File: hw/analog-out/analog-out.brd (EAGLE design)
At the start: 90.2 x 37 mm, 126 parts

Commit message: First verision of dac schematic
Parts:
- removed ADC_: LTC2312, LTC2312-14:TSOT-23_TS8_LIT
- removed ADC_IN, ADC_REF, A_IN, FILTER: TESTPIN, myLib:1X01
- removed ANALOG_IN: PTR1B1,27, testpad:B1,27
- removed C15, C18, C19: 2u2, rcl:C0805K
- removed C8: 100n, rcl:C0805K
- removed C_FILTER: 330p, rcl:C0805K
- removed C_FILTER1: nb, rcl:C0805K
- removed INSTR_AMP: AD8250ARMZ, parts:RM_10_ADI
- removed LED2: GREEN, led:SML0805
- removed MINUS, PLUS: 23.3200-21, CONN_BANANA_JACK_4MM_STAUBLI:CONN_23.3200-21_SBI
- removed MOV1: CV300CVQ300K10BL1, myLib:CVQ300K10
- removed PIN_HEADER_SMD: (no value), SMD10_2_pinheader:MA05-2
- removed R11: 0, rcl:R0805
- removed R12: 47k, rcl:R0805
- removed R13: inf, rcl:R0805
- removed R14, R_FILTER1: nb, rcl:R0805
- removed R53, R57, R58: nb, rcl:R1206
- removed R_FILTER: 2k2, rcl:R0805
- added C27: 10p, rcl:C0805
- added C28, C29: 100n, rcl:C0805
- added CONV1: PTR1B1,27, testpad:B1,27
- added POWER1: gr, led:SML0805
- added R23: 680, resistor:R0805
- added U$3: ADA4522-2ARZ-RL, my:MSOP8
- added U$4: MAX1036EKA+T, my:SOT23-8L
- added U$5: 73099RED, my:4MM_BANANA
- added U$6: 73099BLACK, my:4MM_BANANA
- C5: device rcl:C0805K -> rcl:C0805
- R10: value 390k -> tbd
- R3: value 680 -> tbd
- R4, R5: value nb -> tbd; device rcl:R1206 -> rcl:R0805
- U$1: value 0508.500MXEP -> LTC2642IMS-16; device 0508.500MXEP.FUSE:0508.500MXEP -> my:MSOP10
- moved R10 100.7 mm to (-38.2, -48.8), turned to 0 degrees
- moved R3 94.5 mm to (-38.2, -42.5), flipped to the top
- moved R19 91.9 mm to (57.4, 20.4), turned to 90 degrees
- moved C5 87.1 mm to (-38.2, -36.3), flipped to the top, turned to 0 degrees
- moved R18 86.5 mm to (55.2, 20.4), turned to 90 degrees
- moved R5 72.4 mm to (-30.7, -30.1), turned to 0 degrees
- moved R8 71.3 mm to (35.6, 26.8), turned to 180 degrees
- moved R4 58.2 mm to (-30.7, -23.9), turned to 0 degrees
- moved U$1 46.3 mm to (-21.6, 1.02), turned to 0 degrees
- moved R22 42.2 mm to (70.5, 16.6)
- moved R20 34.4 mm to (71.1, 21.3), turned to 90 degrees
- moved STATUS 31.0 mm to (42.2, 18.5), turned to 180 degrees
- moved +5V 10.2 mm to (50.0, 29.5)
- moved C6 7.39 mm to (69.1, 22.0), turned to 90 degrees
- moved GOLD_ORB_SM1 2.74 mm to (40.8, 30.1), turned to 180 degrees
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- renumbered REF_2.048 to REF_2.5
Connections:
- removed net >ADC: ADC_.4, ADC_IN.1, C_FILTER.1, R10.2, R11.2, R_FILTER.1
- removed net CONV<: PIN_HEADER_SMD.6, RJ45.5
- removed net CONV>: CONVERSION.2, PIN_HEADER_SMD.1
- removed net GAIN_LSB: INSTR_AMP.4, U$2.11
- removed net GAIN_MSB: INSTR_AMP.5, U$2.12
- removed net N$18: R11.1, R13.2, SATURATION_DETECT.3
- removed net N$20: ANALOG_IN.TP, A_IN.1, R14.2, R4.1, U$20.6
- removed net N$21: R57.1, R58.2
- removed net N$29: R4.2, R53.1
- removed net N$4: I2C.3, R18.1, ROHM_I2C.6, U$2.14
- removed net N$6: I2C.2, R19.1, ROHM_I2C.5, U$2.15
- removed net N$66: R53.2, R58.1
- removed net N$67: R5.1, R57.2
- removed net N$8: ADC_.2, ADC_REF.1, C19.2
- removed net N_STATUS_LED: R8.1, U$2.6
- removed net SAT_DETECT: R3.1, SATURATION_DETECT.1, SATURATION_DETECT.6, U$2.10
- removed net SCL<: PIN_HEADER_SMD.5, RJ45.7
- removed net SCL>: I2C.6, PIN_HEADER_SMD.2, R22.1
- removed net SDO<: PIN_HEADER_SMD.4, RJ45.8
- removed net SDO>: I2C.7, PIN_HEADER_SMD.3, R20.1
- new net ANALOG_FEEDBACK: U$20.1, U$4.1
- new net CONV: CONV1.TP, CONVERSION.2, RJ45.5
- new net N$22: R8.1, STATUS.A
- new net N$27: POWER1.A, R23.1
- new net SCL: I2C.6, R22.1, RJ45.7
- new net SDO: I2C.7, R20.1, RJ45.8
- new net STATUS_LED: R8.2, U$2.6
- new net V_OUT: R10.1, R4.2, TP1.TP, TP3.TP, U$3.7, U$5.P$1
- net +5V: now also C28.1, C29.1, C5.1, R23.2, U$1.9, U$3.4, U$4.8; no longer ADC_.1, ADC_.5, C15.1, C18.1, C5.2, INSTR_AMP.8, LED2.A, STATUS.A
- net -5V: now also C28.2, U$3.8; no longer C8.2, INSTR_AMP.3
- net CONV_ADC: now also U$1.2; no longer ADC_.8
- net DGND: now also C29.2, C5.2, POWER1.C, R3.2, R5.2, STATUS.C, U$1.10, U$4.7, U$6.P$1; no longer ADC_.3, C15.2, C18.2, C19.1, C5.1, C8.1, C_FILTER.2, C_FILTER1.2, INSTR_AMP.1, INSTR_AMP.2, MINUS.1, MOV1.2, R12.1, R13.1, R14.1
- net N$1: now also C27.2, U$1.7, U$3.2; no longer INSTR_AMP.7, R_FILTER.2
- net N$14: now also I2C.2, R19.1, ROHM_I2C.5, U$2.15, U$4.6; no longer LED2.C, R3.2
- net N$15: now also R4.1, R5.1, U$3.6; no longer C_FILTER1.1, INSTR_AMP.10, R_FILTER1.1
- net N$16: now also R10.2, R3.1, U$20.6; no longer PLUS.1, TP1.TP, TP3.TP, U$1.P$1
- net N$17: now also I2C.3, R18.1, ROHM_I2C.6, U$2.14, U$4.5; no longer R10.1, R12.2, SATURATION_DETECT.4
- net N$26: now also SCK.2, SCK_A.TP, U$1.3; no longer R8.2, STATUS.C
- net N$5: now also U$1.6, U$3.3; no longer FILTER.1, R_FILTER1.2, U$20.1
- net N$9: now also C27.1, U$1.8, U$3.1, U$3.5; no longer MOV1.1, R5.2, U$1.P$2
- net N_WE: no longer INSTR_AMP.6
- net REF_: now also U$1.1; no longer INSTR_AMP.9
- net SCK_ADC: no longer ADC_.7, SCK.2, SCK_A.TP
- net SDO_ADC: now also U$1.4; no longer ADC_.6
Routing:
- net N$14: track 3.01 -> 43.5 mm
- net N$17: track 2.97 -> 42.3 mm
- net DGND: track 295.8 -> 257.6 mm, vias 38 -> 37
- net N$6: track 37.1 -> 0.00 mm, vias 1 -> 0
- net N$4: track 32.5 -> 0.00 mm, vias 1 -> 0
- net SDO>: track 31.1 -> 0.00 mm, vias 2 -> 0
- net SCL: track 0.00 -> 30.2 mm
- net CONV: track 0.00 -> 26.8 mm, vias 0 -> 1
- net SCL>: track 25.5 -> 0.00 mm
- net SDO: track 0.00 -> 24.0 mm
- net >ADC: track 24.0 -> 0.00 mm
- net INPUT_ZERO: track 0.00 -> 20.0 mm, vias 0 -> 1
- net N$22: track 0.00 -> 19.3 mm, vias 0 -> 2
- net CONV>: track 18.8 -> 0.00 mm, vias 1 -> 0
- net N$16: track 18.2 -> 0.00 mm
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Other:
- board text added: "2022_10_08"
- board text added: "M. Pitz; N. Eiling"
- board text added: "OL"
- board text added: "PWR"
- board text added: "ST"
- board text added: "VILLASsensor V0.2"
- board text removed: "2021_11_05"
- board text removed: "T. Di Raimondo; M. Pitz; N. Eiling"
- board text removed: "VILLASsensor V0.1"

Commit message: first revision of dac board
Signed-off-by: Manuel Pitz <manuel.pitz@eonerc.rwth-aachen.de>
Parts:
- removed 74LVC1G11: SN74LVC1G32DCKT, 74LVC1G11DBV:DBV0006A_L
- removed C16, C17, C21, C26: 100n, rcl:C0805K
- removed CONV_A, CONV_T, GND1, GND2, GND3, SCK_A, SCK_T, SDO_A, SDO_T: PTR1B1,27, testpad:B1,27
- removed FLIP-FLOP: 74HC74PW, 74H74PW:TSSOP14_SOT402-1_NEX
- removed R10: tbd, rcl:R0805
- removed SATURATION_DETECT: ADCMP670, ADCMP670:UJ_6_ADI
- removed SDO: (no value), con-lstb:MA03-1
- removed SN74LVC1G32: 74LVC1G32, SN74LVC1G32:DCK5-M
- removed U$20: MAX4564UMAX, myLib:UMAX8
- added +12V: TESTPIN, myLib:1X01
- added C15, C18, C19: tbd, rcl:C0805K
- added C8: 1u, rcl:C0805K
- added CONV_TP, SCK_TP, SDA_TP: PTR1B1,27, testpad:B1,27
- added R11: 10k, rcl:RTRIMT93YA
- added R12: 100, resistor:R0805
- added SDA: (no value), jumper:JP1
- added U$11: MAX4659, my:UMAX8
- added U$7: LDO_MIC5233-5.0YM5-TR, my:SOT23-5
- added U$8, U$9: 4u7, my:L5038P
- C2: value 100n -> 1u
- C20: value 100n -> tbd
- C22, C25: device rcl:C0805K -> rcl:C0805
- CONV, SCK: device con-lstb:MA03-1 -> jumper:JP1
- R3: value tbd -> 1k
- R4: value tbd -> 10k; device rcl:R0805 -> rcl:RTRIMT93YA
- R5: value tbd -> 2k2
- moved C5 96.1 mm to (36.8, 23.7), flipped to the bottom, turned to 180 degrees
- moved R3 90.8 mm to (24.1, 23.5), flipped to the bottom, turned to 180 degrees
- moved U$4 90.8 mm to (36.8, 22.7)
- moved R5 68.4 mm to (18.9, 16.9), flipped to the bottom
- moved R4 67.6 mm to (21.1, 19.6), turned to 90 degrees
- moved C29 62.5 mm to (25.0, 10.5), turned to 180 degrees
- moved C27 59.7 mm to (25.1, 15.7), turned to 180 degrees
- moved C28 54.5 mm to (18.7, 11.6), turned to 180 degrees
- moved U$3 49.7 mm to (18.8, 14.2), turned to 90 degrees
- moved U$1 48.3 mm to (25.1, 13.2), turned to 90 degrees
- moved GND5 22.8 mm to (35.9, 35.9)
- moved GOLD_ORB_SM1 17.7 mm to (37.0, 12.8), turned to 0 degrees
- moved C22 15.3 mm to (29.6, 22.2), flipped to the bottom, turned to 180 degrees
- moved C2 14.1 mm to (40.5, 31.2)
- moved C1 12.0 mm to (30.5, 6.86), turned to 0 degrees
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- renumbered -5V to -12V
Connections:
- removed net -5V: -12V.1, C17.2, C21.2, C24.2, C28.2, DC-DC_CONVERTER.5, U$20.3, U$3.8
- removed net ANALOG_FEEDBACK: U$20.1, U$4.1
- removed net N$23: 74LVC1G11.3, FLIP-FLOP.9
- removed net N$25: CONV.3, FLIP-FLOP.2
- removed net N$30: SDO.2, SDO_T.TP, SERIAL_DATA.6
- removed net N$31: SDO.3, SN74LVC1G32.4
- new net +12V: +12V.1, C15.1, C22.2, C28.1, C8.1, U$11.4, U$3.4, U$7.P$1, U$7.P$3, U$8.1
- new net -12V: -12V.1, C20.2, C25.1, C28.2, U$11.7, U$3.8, U$9.1
- new net N$18: R12.2, U$11.1
- new net N$4: SDA.2, SERIAL_DATA.6
- new net N$6: C19.2, C24.2, DC-DC_CONVERTER.5, U$9.2
- net +5V: now also U$1.5, U$7.P$5; no longer 74LVC1G11.5, C16.1, C20.2, C22.1, C25.1, C26.1, C28.1, DC-DC_CONVERTER.7, FLIP-FLOP.1, FLIP-FLOP.10, FLIP-FLOP.13, FLIP-FLOP.14, FLIP-FLOP.4, SATURATION_DETECT.5, SN74LVC1G32.5, U$20.8, U$3.4
- net CONV_ADC: now also CONV_TP.TP; no longer CONV_A.TP, FLIP-FLOP.5, SN74LVC1G32.1
- net DGND: now also C15.2, C18.2, C19.1, C22.1, C8.2, U$11.2, U$11.3, U$4.2, U$4.3, U$4.4, U$7.P$2; no longer 74LVC1G11.2, C16.2, C17.1, C21.1, C22.2, C26.2, FLIP-FLOP.7, GND1.TP, GND2.TP, GND3.TP, SATURATION_DETECT.2, SN74LVC1G32.3, U$20.2, U$20.4, U$20.7
- net INPUT_ZERO: now also U$11.6; no longer U$20.5
- net N$13: now also R12.1, U$4.1; no longer 74LVC1G11.4, SCK.3
- net N$15: now also R4.2; no longer R4.1
- net N$16: now also R11.2, U$11.8; no longer R10.2, U$20.6
- net N$19: now also C18.1, DC-DC_CONVERTER.7, U$8.2; no longer 74LVC1G11.6, FLIP-FLOP.12, FLIP-FLOP.6
- net N$24: no longer CONV_T.TP
- net N$26: now also SCK.1, SCK_TP.TP; no longer SCK.2, SCK_A.TP
- net SCK_ADC: now also SCK.2; no longer 74LVC1G11.1, FLIP-FLOP.11, FLIP-FLOP.3, SCK.1, SCK_T.TP
- net SDO_ADC: now also SDA.1, SDA_TP.TP; no longer SDO.1, SDO_A.TP, SN74LVC1G32.2
- net V_OUT: now also R11.1, R4.3; no longer R10.1, R4.2
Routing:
- net -5V: track 67.0 -> 0.00 mm, vias 3 -> 0
- net +12V: track 0.00 -> 66.9 mm, vias 0 -> 3
- net -12V: track 0.00 -> 61.5 mm, vias 0 -> 3
- net V_OUT: track 0.17 -> 46.8 mm
- net +5V: track 180.7 -> 142.9 mm, vias 17 -> 10
- net N_WE: track 37.2 -> 0.00 mm, vias 1 -> 0
- net DGND: track 257.6 -> 222.0 mm, vias 37 -> 18
- net SCK_ADC: track 40.1 -> 11.8 mm, vias 3 -> 1
- net N$31: track 17.9 -> 0.00 mm
- net INPUT_ZERO: track 20.0 -> 2.47 mm
- net N$26: track 11.3 -> 28.5 mm, vias 0 -> 1
- net N$9: track 0.00 -> 15.5 mm, vias 0 -> 2
- net N$30: track 14.0 -> 0.00 mm
- net N$14: track 43.5 -> 57.5 mm, vias 1 -> 2
- net N$17: track 42.3 -> 55.4 mm, vias 1 -> 2
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- removed copper zone on layer 1, net DGND
- removed copper zone on layer 16, net DGND
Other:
- board text added: "2023_14_08"
- board text added: "VILLASdac V0.1"
- board text removed: "100mA, 250V"
- board text removed: "2022_10_08"
- board text removed: "Jumper für I2C und CONV durch testpads ersetzen"
- board text removed: "Lan port 3mm raus ✓"
- board text removed: "Power led weiter links (oder über den lan port)"
- board text removed: "Rechte Holes weiter rein"
- board text removed: "Sicherungen und abständer an + prüfen"
- board text removed: "VILLASsensor V0.2"
- board text removed: "https://de.rs-online.com/web/p/led-lichtleiter/8796453"

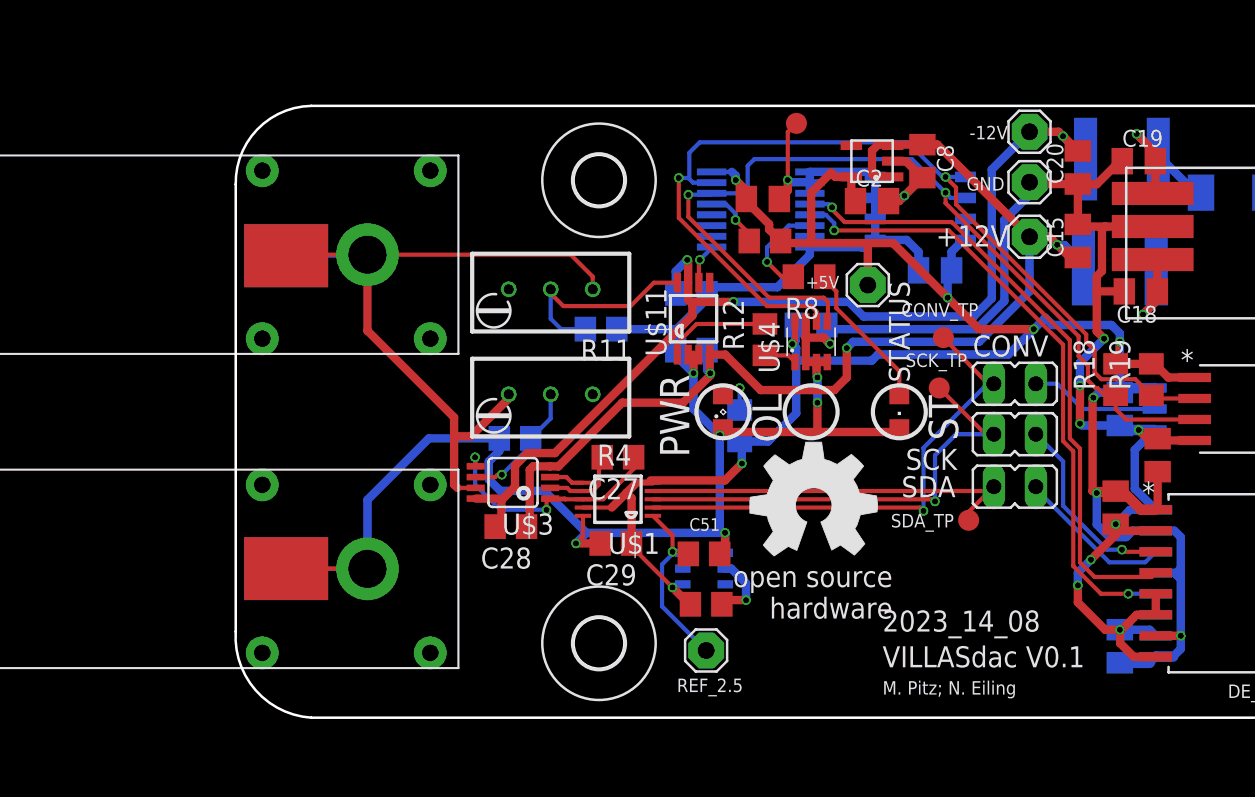
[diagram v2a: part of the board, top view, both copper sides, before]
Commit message: add polygon
Signed-off-by: Manuel Pitz <manuel.pitz@eonerc.rwth-aachen.de>
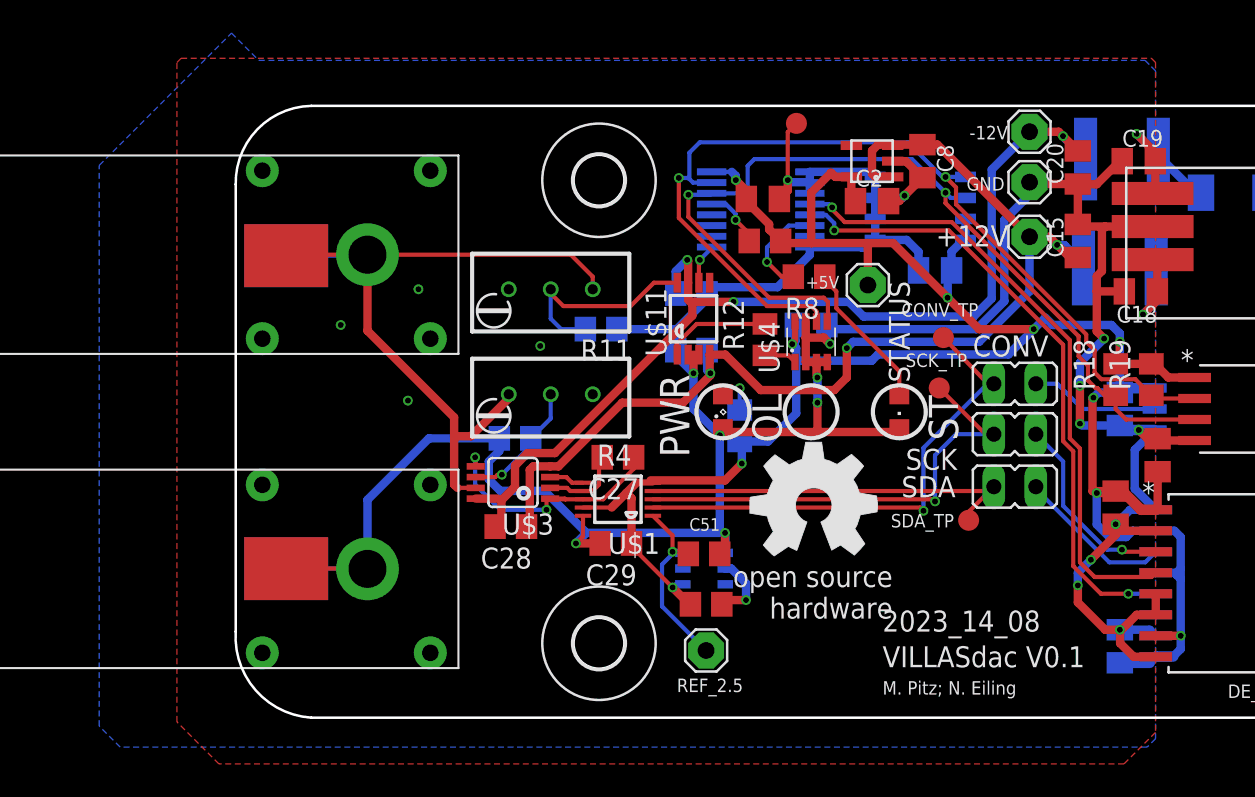
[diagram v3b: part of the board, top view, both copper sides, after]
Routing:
- net DGND: vias 18 -> 22
- added copper zone on layer 1, net DGND
- added copper zone on layer 16, net DGND
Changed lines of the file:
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@@
 <drawing>
 <settings>
-<setting alwaysvectorfont="yes"/>
+<setting alwaysvectorfont="no"/>
 <setting verticaltext="up"/>
 </settings>
@@
 <wire x1="55.499" y1="5.318" x2="55.5141" y2="5.3029" width="0.508" layer="1"/>
 <wire x1="55.499" y1="5.318" x2="55.5545" y2="5.2625" width="0.508" layer="1"/>
+<polygon width="0.1524" layer="1">
+<vertex x="-1.27" y="39.878"/>
+<vertex x="57.404" y="39.878"/>
+<vertex x="57.658" y="39.624"/>
+<vertex x="57.658" y="-0.889"/>
+<vertex x="55.753" y="-2.794"/>
+<vertex x="1.016" y="-2.794"/>
+<vertex x="-1.524" y="-0.254"/>
+<vertex x="-1.524" y="39.624"/>
+</polygon>
+<polygon width="0.1524" layer="16">
+<vertex x="1.778" y="41.402"/>
+<vertex x="3.429" y="39.751"/>
+<vertex x="50.927" y="39.751"/>
+<vertex x="57.023" y="39.751"/>
+<vertex x="57.404" y="39.37"/>
+<vertex x="57.531" y="39.243"/>
+<vertex x="57.658" y="39.116"/>
+<vertex x="57.658" y="-1.27"/>
+<vertex x="57.15" y="-1.778"/>
+<vertex x="-4.953" y="-1.778"/>
+<vertex x="-6.223" y="-0.508"/>
+<vertex x="-6.223" y="33.401"/>
+</polygon>
+<via x="13.081" y="25.908" extent="1-16" drill="0.35"/>
+<via x="20.447" y="22.479" extent="1-16" drill="0.35"/>
+<via x="8.382" y="23.749" extent="1-16" drill="0.35"/>
+<via x="12.446" y="19.177" extent="1-16" drill="0.35"/>
 </signal>
 <signal name="CLK-">

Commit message: updated version of board and schematic
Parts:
- added DGND_1, DGND_2: PTR1B1,27, testpad:B1,27
- added DGND_5, DGND_6: TESTPIN, myLib:1X01
- R12: value 100 -> 1k
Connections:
- net DGND: now also DGND_1.TP, DGND_2.TP, DGND_5.1, DGND_6.1
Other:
- board text added: "2023_08_15"
- board text added: "DINOdac V0.1"
- board text added: "TDN3 1222 WISM"
- board text removed: "2023_14_08"
- board text removed: "VILLASdac V0.1"

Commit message: hw: change isolator to si8400ab
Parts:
- I2C: value ADUM1250 -> SI8400AB-B-IS
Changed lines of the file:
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@@
 <drawing>
 <settings>
-<setting alwaysvectorfont="yes"/>
+<setting alwaysvectorfont="no"/>
 <setting verticaltext="up"/>
 </settings>
@@
 <attribute name="VENDOR" value="Traco Power" x="16.764" y="61.722" size="1.778" layer="27" rot="R180" display="off"/>
 </element>
-<element name="I2C" library="ADUM1251WARZ" package="R_8_ADI" value="ADUM1250" x="62.484" y="18.669" smashed="yes">
+<element name="I2C" library="ADUM1251WARZ" package="R_8_ADI" value="SI8400AB-B-IS" x="62.484" y="18.669" smashed="yes">
 <attribute name="BUILT_BY" value="EMA_UL_Team" x="113.284" y="-25.781" size="1.778" layer="27" display="off"/>
 <attribute name="COPYRIGHT" value="Copyright (C) 2018 Accelerated Designs. All rights reserved" x="113.284" y="-25.781" size="1.778" layer="27" display="off"/>
